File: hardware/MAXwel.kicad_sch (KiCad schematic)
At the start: 155 parts, among them J1 Conn_02x05_Odd_Even, J2 Conn_02x12_Counter_Clockwise, J3 Barrel_Jack_Switch_Pin3Ring, SW1 SW_Push_Dual, SW10 SW_Wuerth_450301014042, SW11 SW_Wuerth_450301014042, SW12 SW_Wuerth_450301014042, SW13 SW_Wuerth_450301014042, SW2 SW_Push_Dual, SW3 SW_Push_Dual, SW4 SW_Push_Dual, SW5 SW_Wuerth_450301014042, SW6 SW_Wuerth_450301014042, SW7 SW_Wuerth_450301014042, SW8 SW_Wuerth_450301014042, SW9 SW_Push_DPDT, U1 D168K, U2 D168K, U3 D168K, U4 D168K, U5 EPM240T100, U6 AMS1117-3.3, X1 50.000, X2 14.756

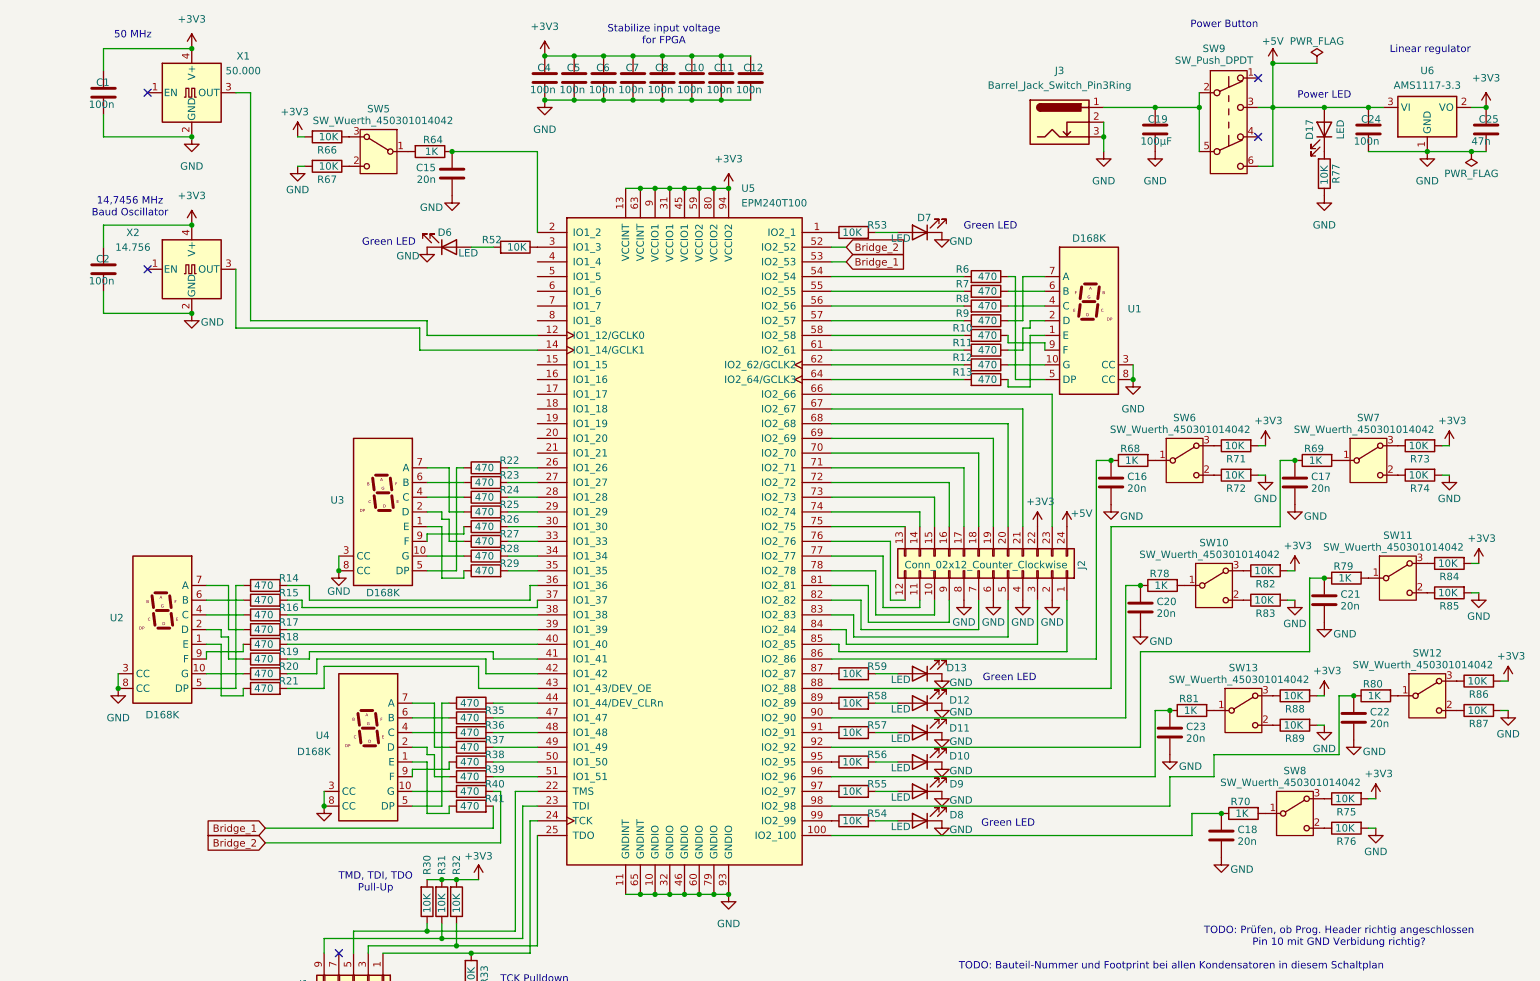
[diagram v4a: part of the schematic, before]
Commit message: shifted everything 1 pin to the side for better power routing
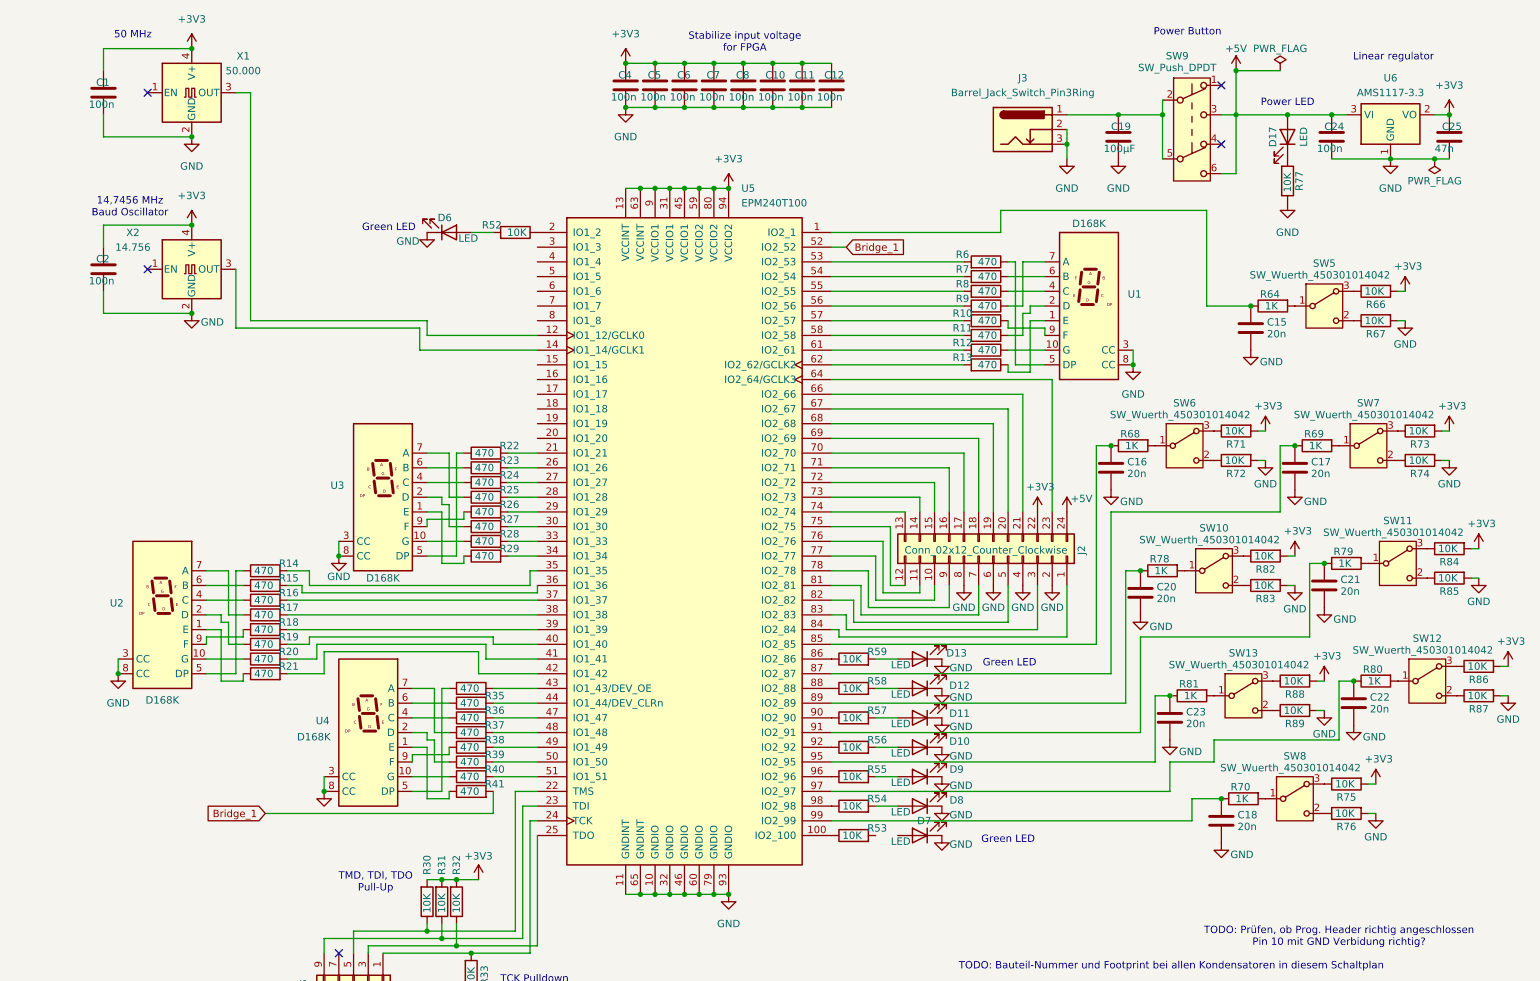
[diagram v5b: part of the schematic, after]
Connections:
- net Bridge_1: now also U5.52 (IO2_52); no longer U5.53 (IO2_53)
- net at C15.1, R64.1: now also U5.1 (IO2_1); no longer U5.2 (IO1_2)
- net at R18.2: now also U5.39 (IO1_39); no longer U5.40 (IO1_40)
- net at C20.1, R78.1: now also U5.89 (IO2_89); no longer U5.90 (IO2_90)
- net at R59.1: now also U5.86 (IO2_86); no longer U5.87 (IO2_87)
- net at C17.1, R69.1: now also U5.87 (IO2_87); no longer U5.88 (IO2_88)
- net at R17.2: now also U5.38 (IO1_38); no longer U5.39 (IO1_39)
- net at C16.1, R68.1: now also U5.85 (IO2_85); no longer U5.86 (IO2_86)
- net at R35.2: now also U5.44 (IO1_44/DEV_CLRn); no longer U5.47 (IO1_47)
- net at C22.1, R80.1: now also U5.97 (IO2_97); no longer U5.98 (IO2_98)
- net at R53.1: now also U5.100 (IO2_100); no longer U5.1 (IO2_1)
- net at C18.1, R70.1: now also U5.99 (IO2_99); no longer U5.100 (IO2_100)
- net at U5.21 (IO1_21): now also R22.2
- net at U5.26 (IO1_26): now also R23.2; no longer R22.2
- net at U5.27 (IO1_27): now also R24.2; no longer R23.2
- net at U5.28 (IO1_28): now also R25.2; no longer R24.2
- net at U5.29 (IO1_29): now also R26.2; no longer R25.2
- net at R52.1: now also U5.2 (IO1_2); no longer U5.3 (IO1_3)
- net at U5.30 (IO1_30): now also R27.2; no longer R26.2
- net at U5.33 (IO1_33): now also R28.2; no longer R27.2
- net at U5.34 (IO1_34): now also R29.2; no longer R28.2
- net at U5.35 (IO1_35): now also R14.2; no longer R29.2
- net at U5.36 (IO1_36): now also R15.2; no longer R14.2
- net at U5.37 (IO1_37): now also R16.2; no longer R15.2
- net at R19.2: now also U5.40 (IO1_40); no longer U5.41 (IO1_41)
- net at R20.2: now also U5.41 (IO1_41); no longer U5.42 (IO1_42)
- net at R21.2: now also U5.42 (IO1_42); no longer U5.43 (IO1_43/DEV_OE)
- net at R34.2: now also U5.43 (IO1_43/DEV_OE); no longer U5.44 (IO1_44/DEV_CLRn)
- net at R36.2: now also U5.47 (IO1_47); no longer U5.48 (IO1_48)
- net at R37.2: now also U5.48 (IO1_48); no longer U5.49 (IO1_49)
- net at R38.2: now also U5.49 (IO1_49); no longer U5.50 (IO1_50)
- net at R39.2: now also U5.50 (IO1_50); no longer U5.51 (IO1_51)
- net at R6.2: now also U5.53 (IO2_53); no longer U5.54 (IO2_54)
- net at R7.2: now also U5.54 (IO2_54); no longer U5.55 (IO2_55)
- net at R8.2: now also U5.55 (IO2_55); no longer U5.56 (IO2_56)
- net at R9.2: now also U5.56 (IO2_56); no longer U5.57 (IO2_57)
- net at R10.2: now also U5.57 (IO2_57); no longer U5.58 (IO2_58)
- net at R11.2: now also U5.58 (IO2_58); no longer U5.61 (IO2_61)
- net at R12.2: now also U5.61 (IO2_61); no longer U5.62 (IO2_62/GCLK2)
- net at R13.2: now also U5.62 (IO2_62/GCLK2); no longer U5.64 (IO2_64/GCLK3)
- net at J2.23 (Pin_23): now also U5.64 (IO2_64/GCLK3); no longer U5.66 (IO2_66)
- net at J2.21 (Pin_21): now also U5.66 (IO2_66); no longer U5.67 (IO2_67)
- net at J2.20 (Pin_20): now also U5.67 (IO2_67); no longer U5.68 (IO2_68)
- net at J2.19 (Pin_19): now also U5.68 (IO2_68); no longer U5.69 (IO2_69)
- net at J2.18 (Pin_18): now also U5.69 (IO2_69); no longer U5.70 (IO2_70)
- net at J2.17 (Pin_17): now also U5.70 (IO2_70); no longer U5.71 (IO2_71)
- net at J2.16 (Pin_16): now also U5.71 (IO2_71); no longer U5.72 (IO2_72)
- net at J2.15 (Pin_15): now also U5.72 (IO2_72); no longer U5.73 (IO2_73)
- net at J2.14 (Pin_14): now also U5.73 (IO2_73); no longer U5.74 (IO2_74)
- net at J2.13 (Pin_13): now also U5.74 (IO2_74); no longer U5.75 (IO2_75)
- net at J2.12 (Pin_12): now also U5.75 (IO2_75); no longer U5.76 (IO2_76)
- net at J2.11 (Pin_11): now also U5.76 (IO2_76); no longer U5.77 (IO2_77)
- net at J2.10 (Pin_10): now also U5.77 (IO2_77); no longer U5.78 (IO2_78)
- net at J2.9 (Pin_9): now also U5.78 (IO2_78); no longer U5.81 (IO2_81)
- net at J2.7 (Pin_7): now also U5.81 (IO2_81); no longer U5.82 (IO2_82)
- net at J2.5 (Pin_5): now also U5.82 (IO2_82); no longer U5.83 (IO2_83)
- net at J2.3 (Pin_3): now also U5.83 (IO2_83); no longer U5.84 (IO2_84)
- net at J2.1 (Pin_1): now also U5.84 (IO2_84); no longer U5.85 (IO2_85)
- net at R58.1: now also U5.88 (IO2_88); no longer U5.89 (IO2_89)
- net at R57.1: now also U5.90 (IO2_90); no longer U5.91 (IO2_91)
- net at C21.1, R79.1: now also U5.91 (IO2_91); no longer U5.92 (IO2_92)
- net at R56.1: now also U5.92 (IO2_92); no longer U5.95 (IO2_95)
- net at C23.1, R81.1: now also U5.95 (IO2_95); no longer U5.96 (IO2_96)
- net at R55.1: now also U5.96 (IO2_96); no longer U5.97 (IO2_97)
- net at R54.1: now also U5.98 (IO2_98); no longer U5.99 (IO2_99)
- net at D7.2 (A): no longer R53.2
- net Bridge_2: no longer names the net of R40.2
- net Bridge_2: now also U5.51 (IO1_51); no longer U5.52 (IO2_52)
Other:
- moved on the sheet: C10, C11, C12, C15, C16, C17, C18, C19, C20, C21, C22, C23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

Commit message: first successfull redesign
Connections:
- net at C3.1, R42.1: now also U5.20 (IO1_20)
- net at R1.1: now also U5.15 (IO1_15)
- net at U5.16 (IO1_16): now also R62.1
- net at U5.17 (IO1_17): now also R63.1
- net at U5.18 (IO1_18): now also R65.1
- net at U5.19 (IO1_19): now also C9.1, R45.1
- net at U5.3 (IO1_3): now also C14.1, R50.1
- net at U5.4 (IO1_4): now also C13.1, R48.1
- net at U5.5 (IO1_5): now also R2.1
- net at U5.6 (IO1_6): now also R3.1
- net at U5.7 (IO1_7): now also R4.1
- net at U5.8 (IO1_8): now also R5.1
- net at D7.2 (A): now also R53.2
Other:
- moved on the sheet: C1, C10, C11, C12, C13, C14, C15, C16, C17, C18, C19, C2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

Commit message: optimized traces
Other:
- note added: "Wire network: looks cursed but makes routing more efficient"
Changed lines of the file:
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@@
+		)
+	)
+	(text "Wire network:\nlooks cursed but makes\nrouting more efficient"
+		(exclude_from_sim no)
+		(at 61.214 138.938 0)
+		(effects
+			(font
+				(size 1.27 1.27)
+			)
 		)
 	)

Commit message: update sw_slide footprint, added part references and QR code on backside
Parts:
- SW10, SW11, SW12, SW13, SW5, SW6, SW7, SW8: LCSC (none) -> C5155552
- X1: LCSC (none) -> C387308; Part-Nr XO53 50,00000 -> (none)
- X2: LCSC (none) -> C7431374; Part-Nr XO53 14,74560 -> (none)
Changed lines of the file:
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@@
 			)
 		)
+		(property "LCSC" "C5155552"
+			(at 229.87 114.3 0)
+			(effects
+				(font
+					(size 1.27 1.27)
+				)
+				(hide yes)
+			)
+		)
 		(pin "2"
 		)
@@
 			)
 		)
+		(property "LCSC" "C5155552"
+			(at 243.84 153.67 0)
+			(effects
+				(font
+					(size 1.27 1.27)
+				)
+				(hide yes)
+			)
+		)
 		(pin "2"
 		)
@@
 			)
 		)
-		(property "Part-Nr" "XO53 50,00000"
+		(property "LCSC" "C387308"
 			(at 30.48 25.4 0)
 			(effects
@@
 			)
 		)
-		(property "Part-Nr" "XO53 14,74560 "
+		(property "LCSC" "C7431374"
 			(at 30.48 48.26 0)
 			(effects
@@
 			)
 		)
+		(property "LCSC" "C5155552"
+			(at 256.54 92.71 0)
+			(effects
+				(font
+					(size 1.27 1.27)
+				)
+				(hide yes)
+			)
+		)
 		(pin "2"
 		)
@@
 			)
 		)
+		(property "LCSC" "C5155552"
+			(at 224.79 92.71 0)
+			(effects
+				(font
+					(size 1.27 1.27)
+				)
+				(hide yes)
+			)
+		)
 		(pin "2"
 		)
@@
 			)
 		)
+		(property "LCSC" "C5155552"
+			(at 248.92 68.58 0)
+			(effects
+				(font
+					(size 1.27 1.27)
+				)
+				(hide yes)
+			)
+		)
 		(pin "2"
 		)
@@
 			)
 		)
+		(property "LCSC" "C5155552"
+			(at 266.7 133.35 0)
+			(effects
+				(font
+					(size 1.27 1.27)
+				)
+				(hide yes)
+			)
+		)
 		(pin "2"
 		)
@@
 			)
 		)
+		(property "LCSC" "C5155552"
+			(at 261.62 113.03 0)
+			(effects
+				(font
+					(size 1.27 1.27)
+				)
+				(hide yes)
+			)
+		)
 		(pin "2"
 		)
@@
 			(at 234.95 135.89 0)
 			(effects
+				(font
+					(size 1.27 1.27)
+				)
+				(hide yes)
+			)
+		)
+		(property "LCSC" "C5155552"
+			(at 234.95 135.89 0)
+			(effects
